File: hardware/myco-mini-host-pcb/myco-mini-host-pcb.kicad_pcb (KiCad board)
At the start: 2 copper layers, 53.5 x 138.4 mm, 33 parts, among them J1 Conn_01x17_Female, J2 Conn_01x17_Female, Q1 AO3401A, Q2 AO3401A, Q3 AO3401A, Q4 AO3401A, SW1 DM-04-V, SW2 TS-1187A-B-A-B, U1 XC9145B33CMR-G, U2 SHT41-AD1B-R2, U3 BH1750FVI-TR, U4 MAX40203AUK+T

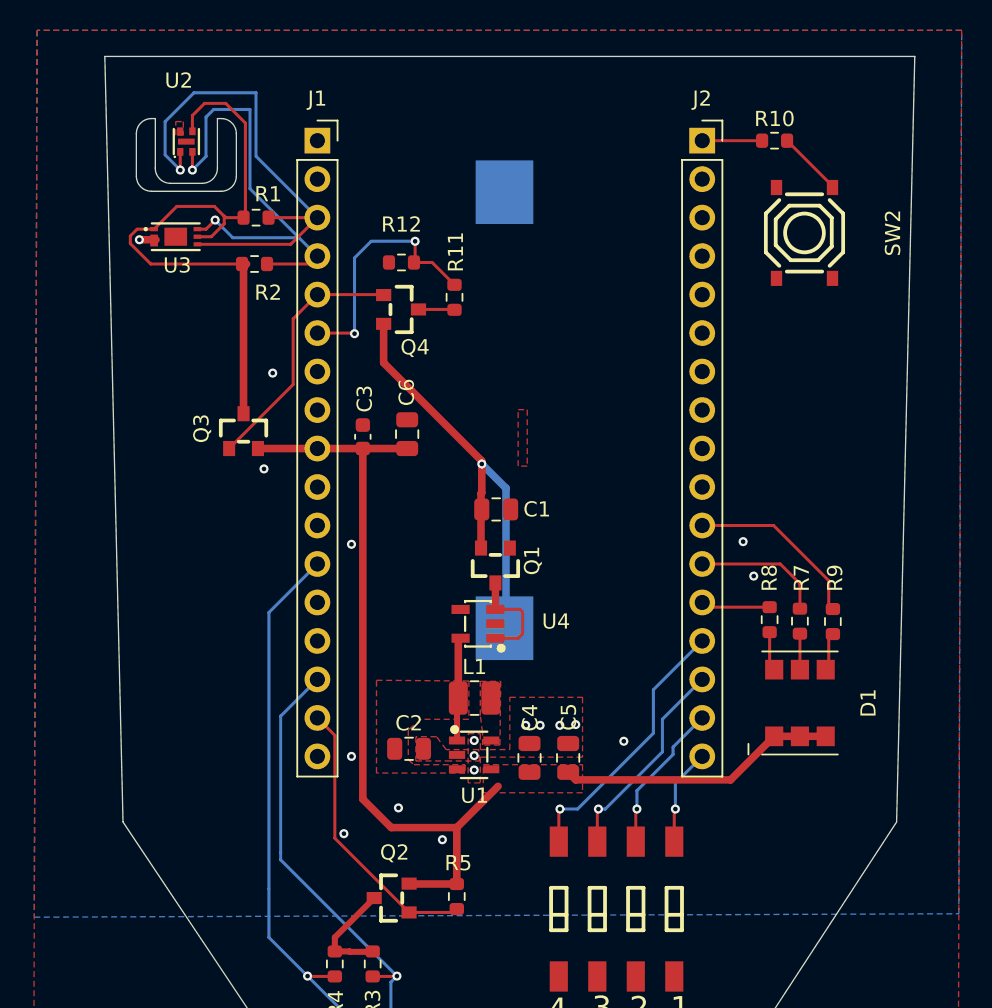
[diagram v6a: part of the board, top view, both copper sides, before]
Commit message: refactor: echange P1.12/P1.13 entre SENSOR_EN et BAT_SENSE
- SENSOR_EN : P1.12 (J1 pin5) -> P1.13 (J1 pin6)
- BAT_SENSE : P1.13 (J1 pin6) -> P1.12 (J1 pin5)

Verifie avant application : P1.12 = AIN5 et P1.13 = AIN6 dans les tables de
brochage du datasheet nRF54L15, donc les deux broches sont capables SAADC.
L'echange est valide dans les deux sens - BAT_SENSE garde une entree
analogique reelle sur P1.12, et SENSOR_EN n'a besoin que d'un GPIO general.

Nets renommes en consequence (P1_12_SENSOR_EN -> P1_13_SENSOR_EN,
P1_13_BAT_SENSE -> P1_12_BAT_SENSE), plus les notes de Q3/Q4 et la BOM.

Alignement des textes preserve : diff UUID sur les 79 labels, zero
deplacement (7 renommages voulus). ERC inchange a 69.

Co-Authored-By: Claude Sonnet 5 <noreply@anthropic.com>
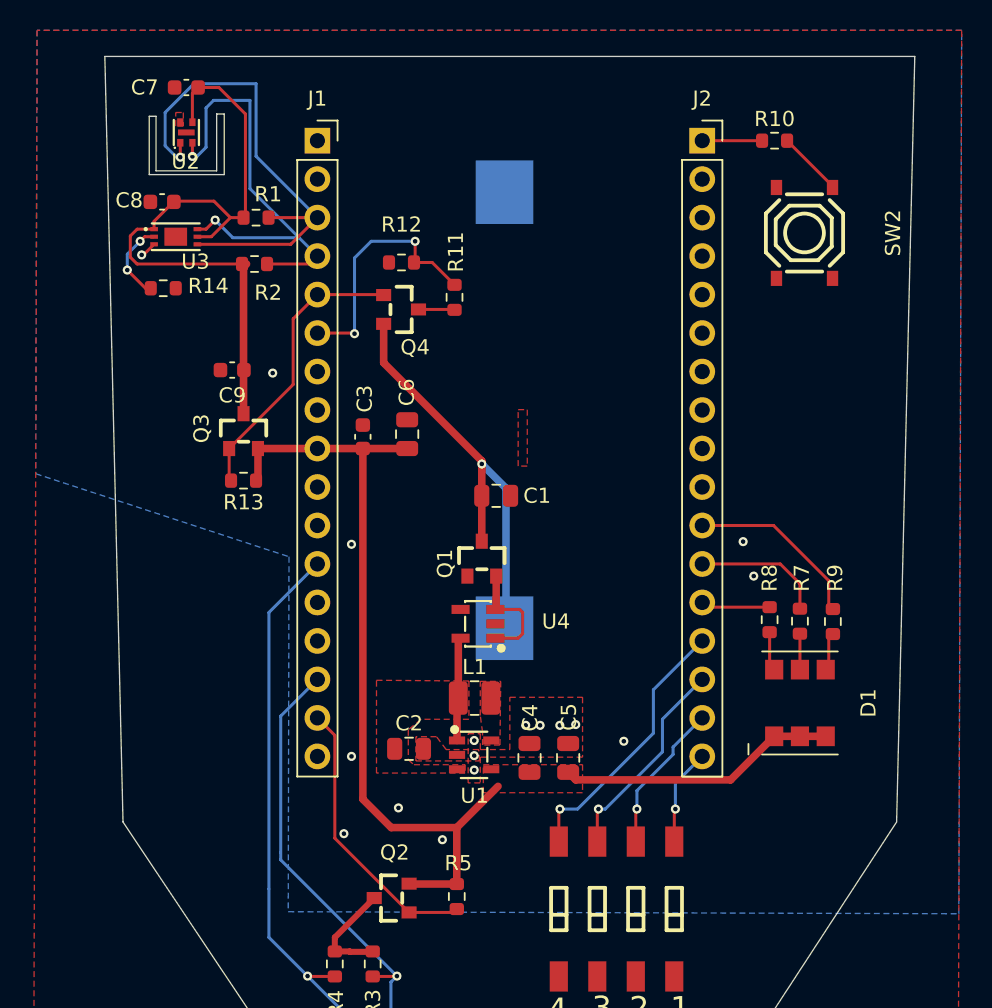
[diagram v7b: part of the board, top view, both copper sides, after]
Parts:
- added C7: 100nF, Capacitor_SMD:C_0603_1608Metric, F.Cu at (56.4, 22.6)
- added C8: 100nF, Capacitor_SMD:C_0603_1608Metric, F.Cu at (54.8, 30.1)
- added C9: 1uF, Capacitor_SMD:C_0603_1608Metric, F.Cu at (59.4, 41.2)
- added R13: 100k, Resistor_SMD:R_0603_1608Metric, F.Cu at (60.2, 48.5)
- added R14: 100k, Resistor_SMD:R_0603_1608Metric, F.Cu at (54.9, 35.8)
- moved Q1 1.01 mm to (75.9, 53.6), turned to -90 degrees
- moved C1 0.90 mm to (76.8, 49.5)
- moved U2 0.60 mm to (56.4, 25.5)
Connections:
- net /P2_04_LED_R renamed /P2_04_LED_G
- net /P2_05_LED_G renamed /P2_05_LED_R
- net /VDD_NRF renamed /BOOST_IN
- J2 pad 3: /P0_03_SCL -> unconnected-(J2-Pin_3-Pad3)
- J2 pad 4: /P0_02_SDA -> unconnected-(J2-Pin_4-Pad4)
- Q1 pad 2: /BAT_RAW -> /VDD_PROT
- Q1 pad 3: /VDD_PROT -> /BAT_RAW
- U2 pad 5: GND -> unconnected-(U2-EP-Pad5)
- U3 pad 2: GND -> Net-(U3-ADDR)
- U3 pad 7: GND -> unconnected-(U3-EP-Pad7)
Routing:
- net Net-(U3-ADDR): track 0.00 -> 5.34 mm, vias 0 -> 2
- net /SENSOR_3V3: track 40.9 -> 43.6 mm
- net /VOUT_3V3: track 69.2 -> 71.3 mm
- net /P1_12_SENSOR_EN: track 17.0 -> 19.1 mm
- net GND: track 1.38 -> 1.11 mm, vias 18 -> 17
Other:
- outline, holes or cut-outs redrawn

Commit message: feat: C6 (100uF) passe de 0805 a 1206 - moins cher et moins de derating
Le 100uF n'existe qu'en 6.3V en boitier 0805, ce qui en faisait le 3e
composant le plus cher de la carte ($0.63, C141660) pour une capacite
effective fortement reduite par le derating DC bias a 3.3V.

En 1206 : GRM31CR61A107ME05L (Murata, C312983) a $0.3505 (MOQ 5, 81k en
stock) et surtout en 10V au lieu de 6.3V, donc bien moins de derating a
3.3V - on paie moins cher pour plus de capacite reelle.

Empreinte du schema passee a Capacitor_SMD:C_1206_3216Metric (verifie que
les autres condensateurs 0805 ne sont pas affectes). Placement PCB a faire
par l'utilisateur, qui a confirme qu'il y a la place a l'emplacement actuel.

Passifs + inductance : $1.19 -> $0.91/carte.

Co-Authored-By: Claude Sonnet 5 <noreply@anthropic.com>
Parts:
- moved R11 8.83 mm to (80.5, 42.5)
- moved Q4 8.83 mm to (77.0, 43.2)
- moved R12 8.52 mm to (77.1, 39.6), turned to 90 degrees
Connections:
- J1 pad 5: /P1_12_SENSOR_EN -> /P1_12_BAT_SENSE
- J1 pad 6: /P1_13_BAT_SENSE -> /P1_13_SENSOR_EN
- Q3 pad 1: /P1_12_SENSOR_EN -> /P1_13_SENSOR_EN
- Q4 pad 1: /P1_12_SENSOR_EN -> /P1_13_SENSOR_EN
- R11 pad 2: /P1_13_BAT_SENSE -> /P1_12_BAT_SENSE
- R12 pad 1: /P1_13_BAT_SENSE -> /P1_12_BAT_SENSE
- R13 pad 2: /P1_12_SENSOR_EN -> /P1_13_SENSOR_EN
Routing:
- net /P1_13_SENSOR_EN: track 0.00 -> 24.5 mm
- net /P1_12_SENSOR_EN: track 19.1 -> 0.00 mm
- net /P1_12_BAT_SENSE: track 0.00 -> 17.7 mm
- net /P1_13_BAT_SENSE: track 16.6 -> 0.00 mm, vias 2 -> 0
- net /BAT_RAW: track 28.6 -> 19.9 mm
- net GND: vias 17 -> 20
